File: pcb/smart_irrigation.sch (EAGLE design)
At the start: 27 parts, among them IC1 7805DT, IC2 7833DT, IC3 TMP36, J1 1X2-3.5MM, Q2 32.768

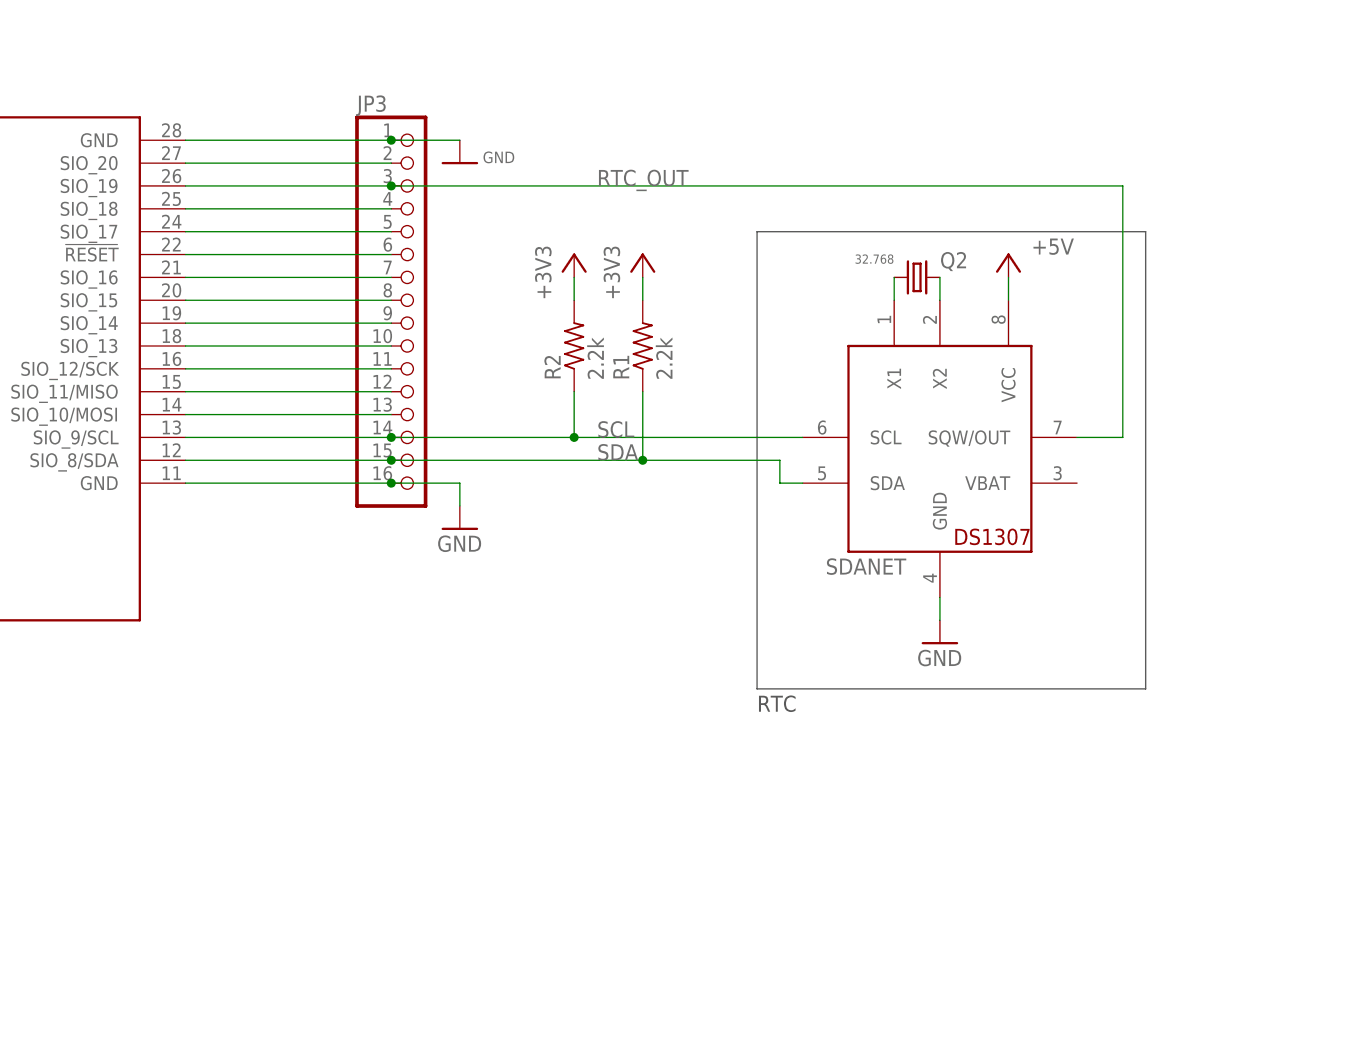
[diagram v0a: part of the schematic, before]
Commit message: PCB: Add solenoid and flow sensor
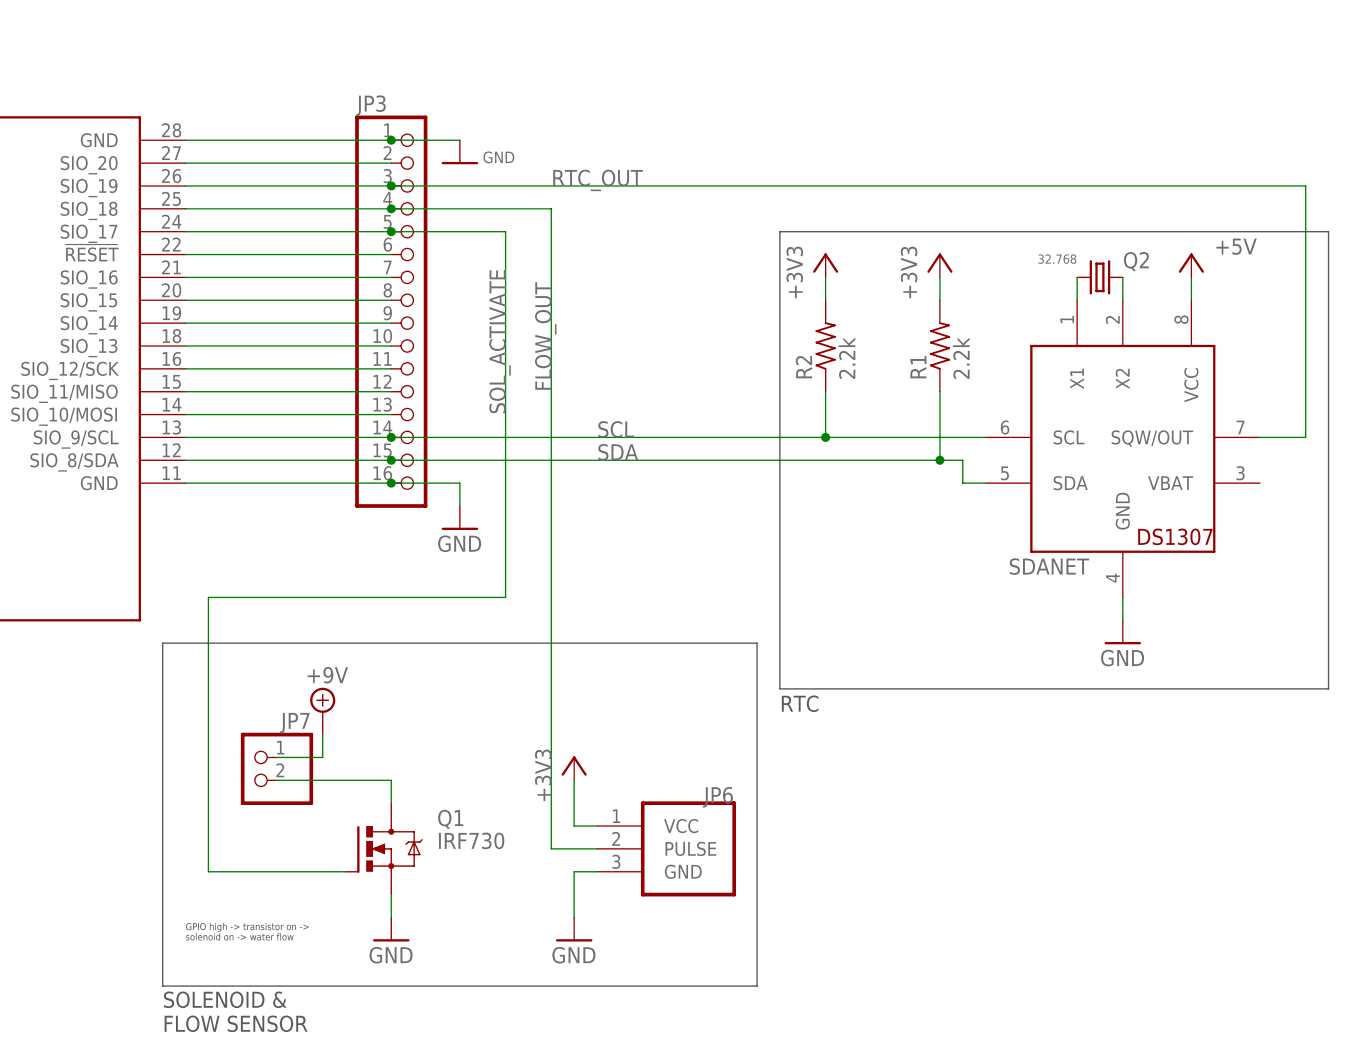
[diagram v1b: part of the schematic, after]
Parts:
- added JP6: (no value), smart_irrigation:FLOW
- added JP7: (no value), pinhead:PINHD-1X2
- added Q1: IRF730, smart_irrigation:IRF730
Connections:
- removed net N$18: JP3.4, U$1.SIO_18
- removed net N$19: JP3.5, U$1.SIO_17
- new net FLOW_OUT: JP3.4, JP6.PULSE, U$1.SIO_18
- new net N$1: JP7.2, Q1.D
- new net SOL_ACTIVATE: JP3.5, Q1.G, U$1.SIO_17
- net +3V3: now also JP6.VCC
- net +9V: now also JP7.1
- net GND: now also JP6.GND, Q1.S
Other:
- note added: "GPIO high -> transistor on -> solenoid on -> water flow"
- note added: "SOLENOID & FLOW SENSOR"
- moved on the sheet: Q2, R1, R2, SDANET

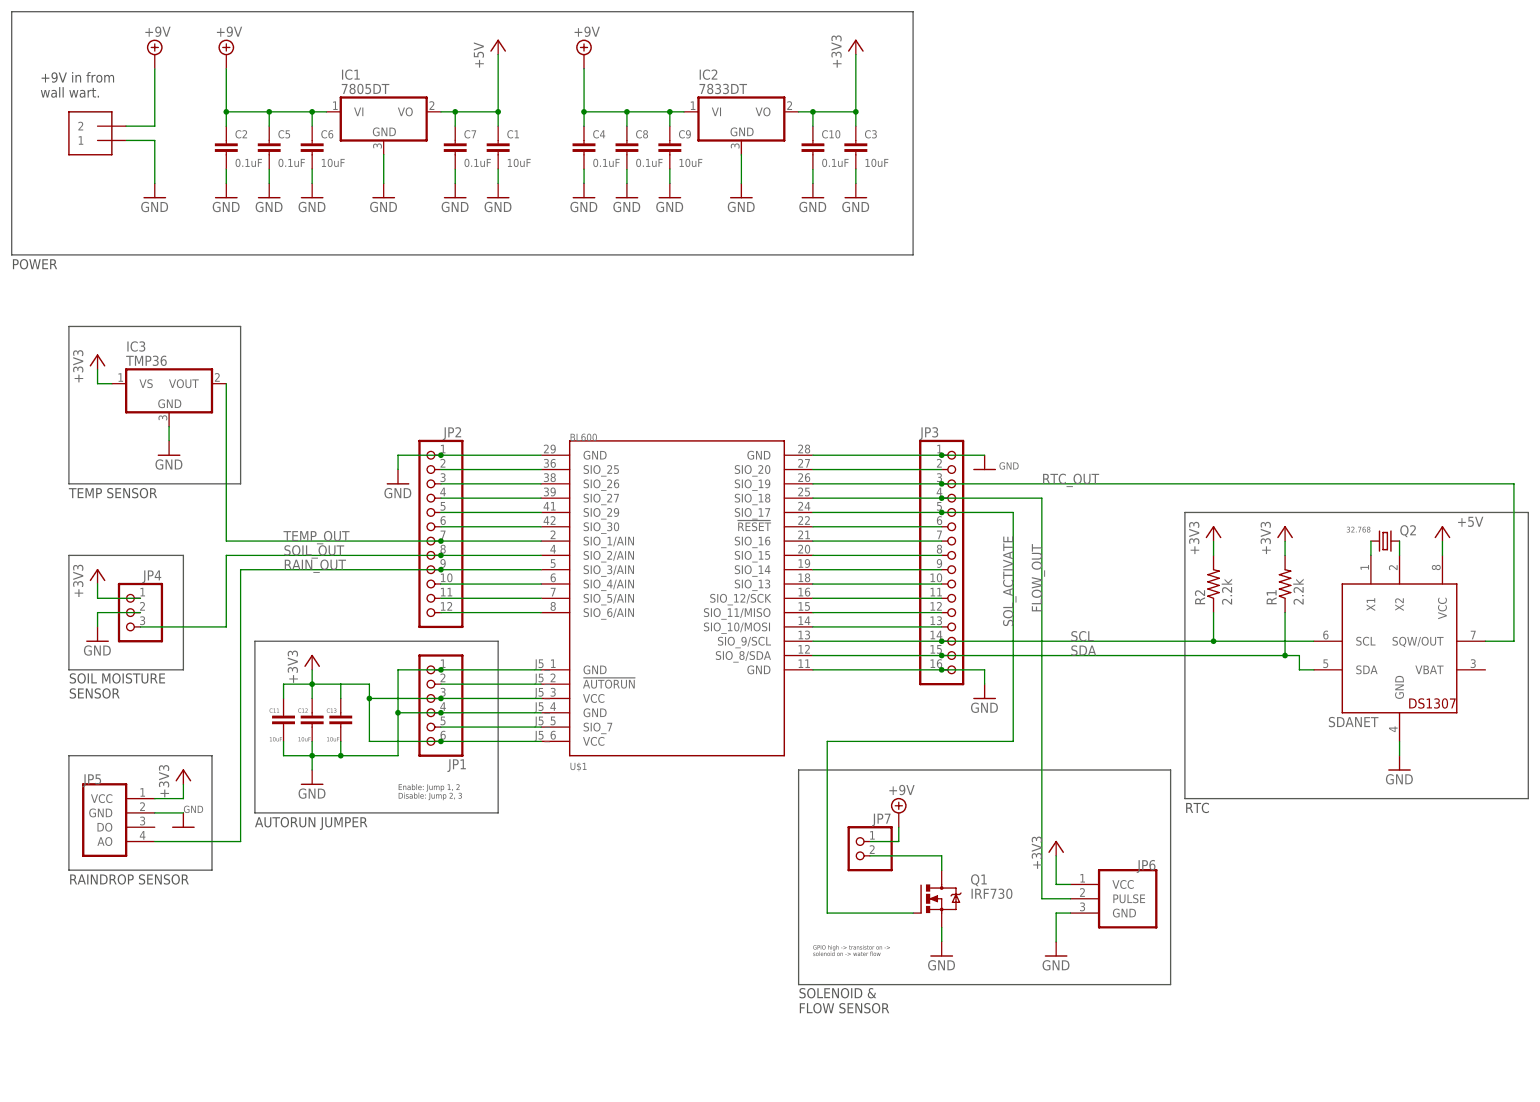
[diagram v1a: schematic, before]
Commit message: PCB: Add transistor to toggle sensors
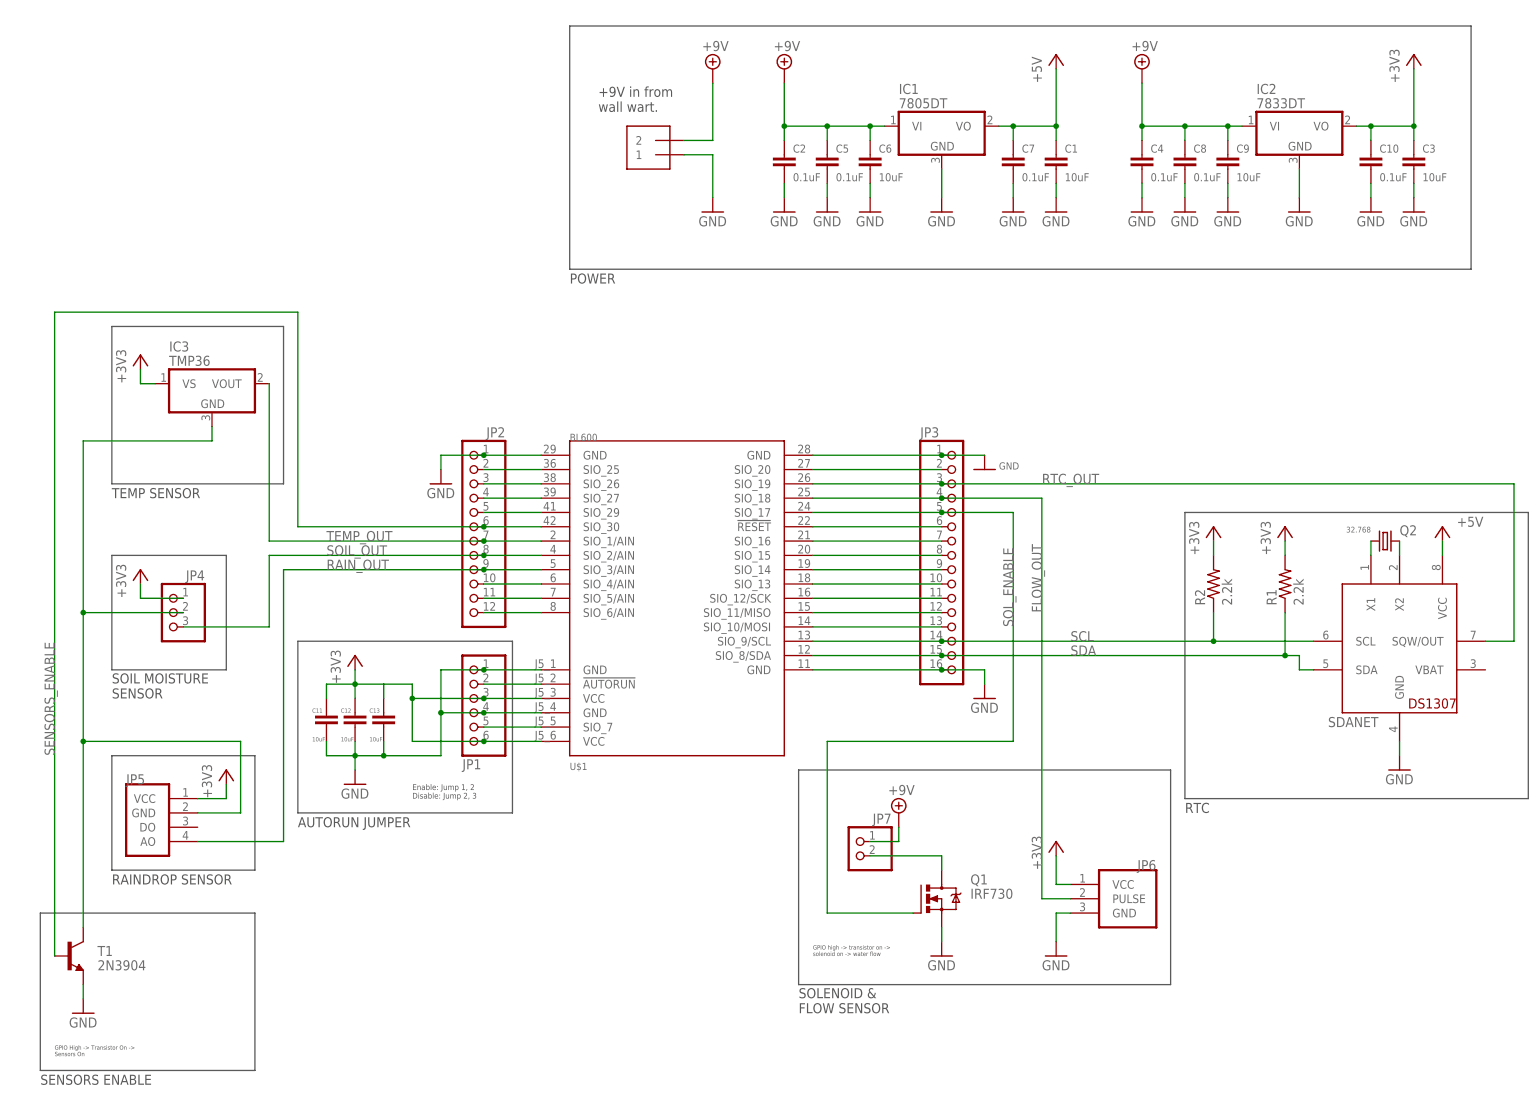
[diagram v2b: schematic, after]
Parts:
- added T1: 2N3904, transistor:2N3904
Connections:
- net SOL_ACTIVATE renamed SOL_ENABLE
- removed net N$8: JP2.6, U$1.SIO_30
- new net 3V3_TRAN_COL: IC3.GND, JP4.2, JP5.GND, T1.C
- new net SENSORS_ENABLE: JP2.6, T1.B, U$1.SIO_30
- net GND: now also T1.E; no longer IC3.GND, JP4.2, JP5.GND
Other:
- note added: "GPIO High -> Transistor On -> Sensors On"
- note added: "SENSORS ENABLE"
- moved on the sheet: C1, C10, C11, C12, C13, C2, C3, C4, C5, C6, C7, C8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

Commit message: PCB: Initial board layout
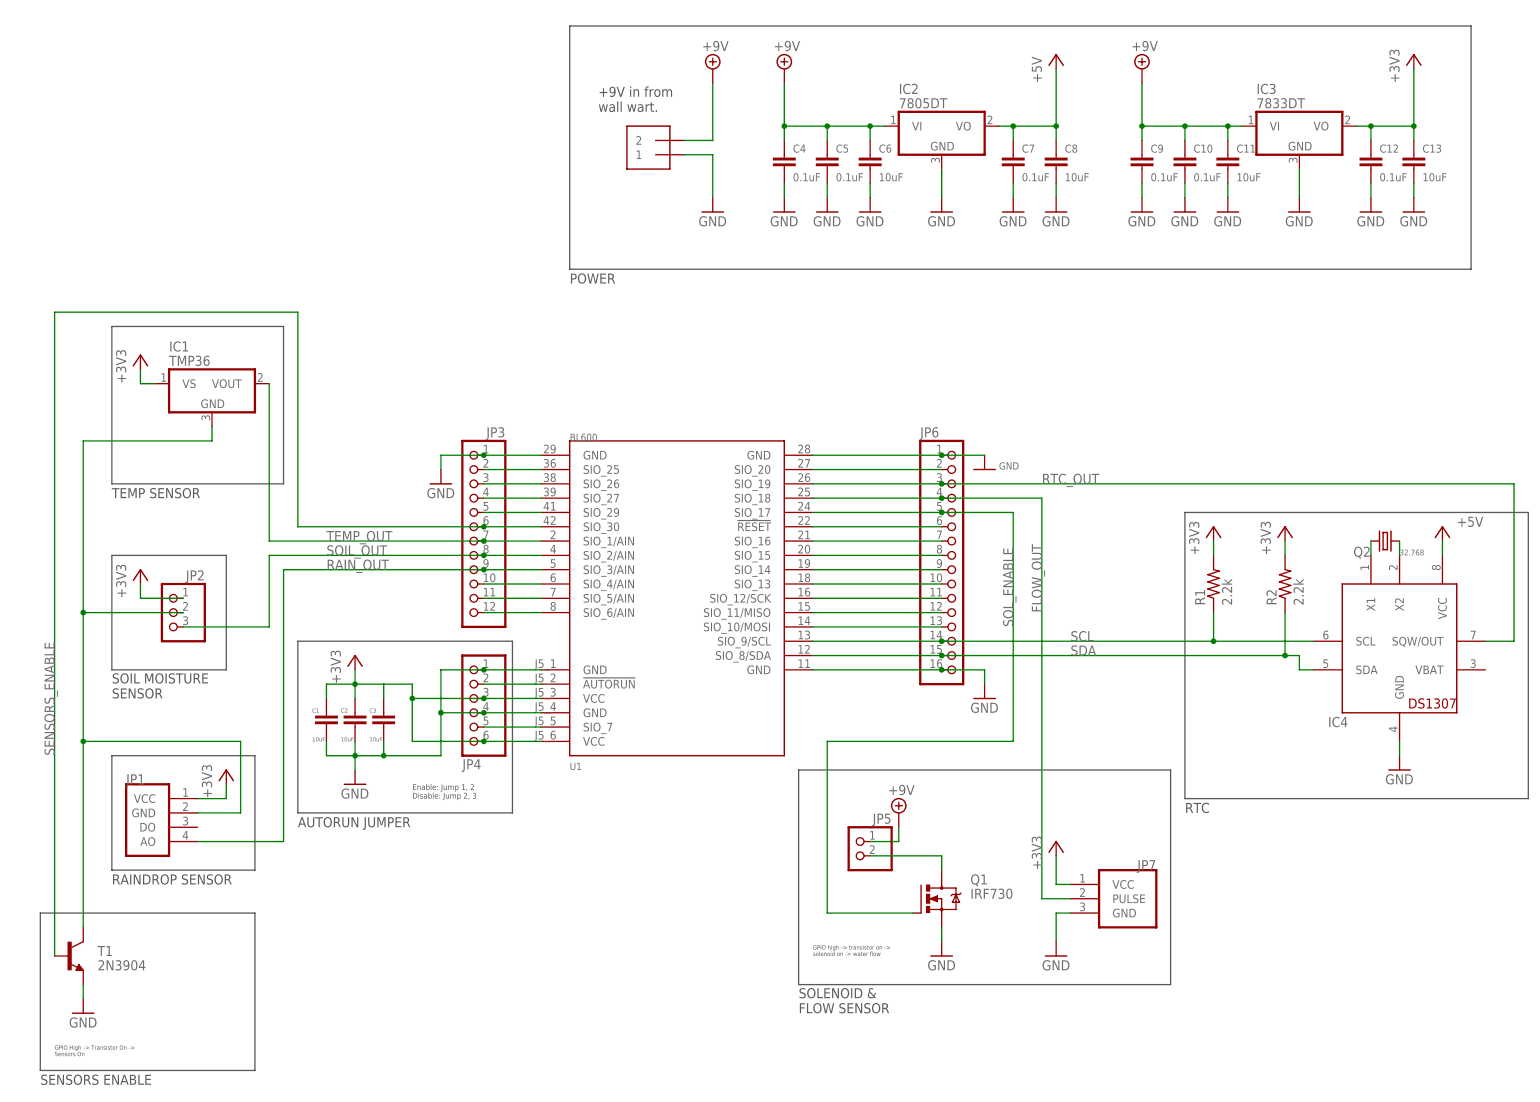
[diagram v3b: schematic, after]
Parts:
- C12, C9: value 10uF -> 0.1uF
- C2, C8: value 0.1uF -> 10uF
- IC1: value 7805DT -> TMP36; device linear:7805DT -> smart_irrigation:TMP36
- IC2: value 7833DT -> 7805DT; device smart_irrigation:7833DT -> linear:7805DT
- IC3: value TMP36 -> 7833DT; device smart_irrigation:TMP36 -> smart_irrigation:7833DT
- JP1: device pinhead:PINHD-1X6 -> smart_irrigation:RAINDROP
- JP2: device pinhead:PINHD-1X12 -> pinhead:PINHD-1X3
- JP3: device pinhead:PINHD-1X16 -> pinhead:PINHD-1X12
- JP4: device pinhead:PINHD-1X3 -> pinhead:PINHD-1X6
- JP5: device smart_irrigation:RAINDROP -> pinhead:PINHD-1X2
- JP6: device smart_irrigation:FLOW -> pinhead:PINHD-1X16
- JP7: device pinhead:PINHD-1X2 -> smart_irrigation:FLOW
- renumbered SDANET to IC4, U$1 to U1
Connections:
- removed net N$15: IC4.X2, Q2.2
- new net SOL_DRAIN: JP5.2, Q1.D
- net +3V3: now also C1.1, C2.1, IC1.VS, IC3.VO, JP1.VCC, JP2.1, JP4.3, JP4.6, JP7.VCC; no longer C10.1, C11.1, IC2.VO, IC3.VS, JP1.3, JP1.6, JP4.1, JP5.VCC, JP6.VCC
- net +5V: now also C8.1, IC2.VO; no longer C1.1, IC1.VO
- net +9V: now also C10.1, C11.1, IC3.VI, JP5.1; no longer C2.1, C8.1, IC1.VI, JP7.1
- net 3V3_TRAN_COL: now also IC1.GND, JP1.GND, JP2.2; no longer IC3.GND, JP4.2, JP5.GND
- net FLOW_OUT: now also JP6.4, JP7.PULSE; no longer JP3.4, JP6.PULSE
- net GND: now also IC3.GND, JP4.1, JP4.4, JP6.1, JP6.16, JP7.GND; no longer IC1.GND, JP1.1, JP1.4, JP2.1, JP3.16, JP6.GND
- net N$1: now also IC4.X1, Q2.2; no longer JP7.2, Q1.D
- net N$12: now also JP3.10; no longer JP2.10
- net N$13: now also JP3.11; no longer JP2.11
- net N$14: now also JP3.12; no longer JP2.12
- net N$16: now also JP6.2; no longer JP3.2
- net N$2: now also JP4.5; no longer JP1.5
- net N$20: now also JP6.6; no longer JP3.6
- net N$21: now also JP6.7; no longer JP3.7
- net N$22: now also JP6.8; no longer JP3.8
- net N$23: now also JP6.9; no longer JP3.9
- net N$24: now also JP6.10; no longer JP3.10
- net N$25: now also JP6.11; no longer JP3.11
- net N$26: now also JP6.12; no longer JP3.12
- net N$27: now also JP6.13; no longer JP3.13
- net N$3: now also IC4.X2; no longer IC4.X1
- net N$4: now also JP3.2; no longer JP2.2
- net N$5: now also JP3.3; no longer JP2.3
- net N$6: now also JP3.4; no longer JP2.4
- net N$7: now also JP3.5; no longer JP2.5
- net NAUTORUN: now also JP4.2; no longer JP1.2
- net RAIN_OUT: now also JP1.AO, JP3.9; no longer JP2.9, JP5.AO
- net RTC_OUT: now also JP6.3; no longer JP3.3
- net SCL: now also JP6.14, R1.1; no longer JP3.14, R2.1
- net SDA: now also JP6.15, R2.1; no longer JP3.15, R1.1
- net SENSORS_ENABLE: now also JP3.6; no longer JP2.6
- net SOIL_OUT: now also JP2.3, JP3.8; no longer JP2.8, JP4.3
- net SOL_ENABLE: now also JP6.5; no longer JP3.5
- net TEMP_OUT: now also IC1.VOUT, JP3.7; no longer IC3.VOUT, JP2.7
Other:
- moved on the sheet: C1, C10, C11, C12, C13, C2, C3, C4, C8, C9, IC1, IC2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
